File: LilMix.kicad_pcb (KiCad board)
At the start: 2 copper layers, 79.6 x 94.4 mm, 59 parts, among them J1_L1 MONO, J1_R1 MONO, J2_L1 MONO, J2_R1 MONO, J3 STEREO, J4 MONO, J5 MONO, J6 STEREO, U1 TL074, U2 NE5532

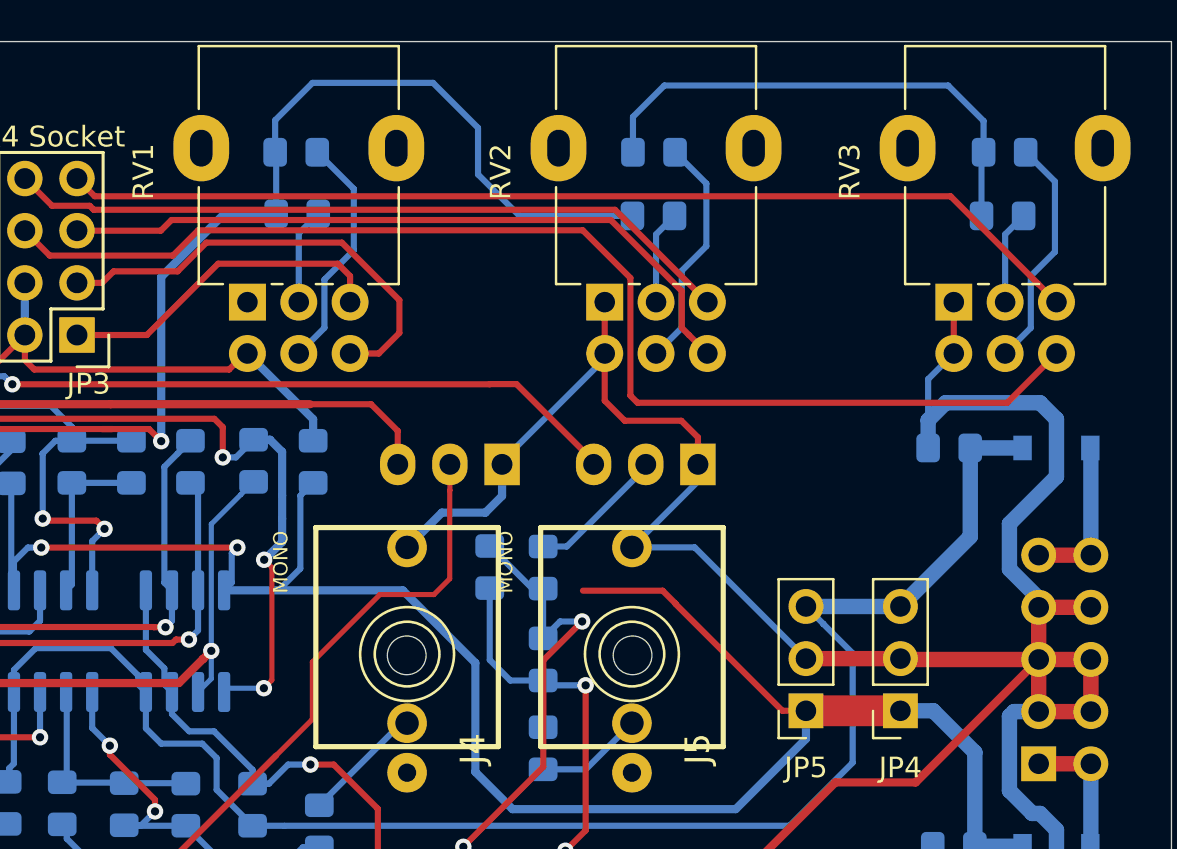
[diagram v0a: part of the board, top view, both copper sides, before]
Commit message: Added another +12v socket header. Initial routing completed
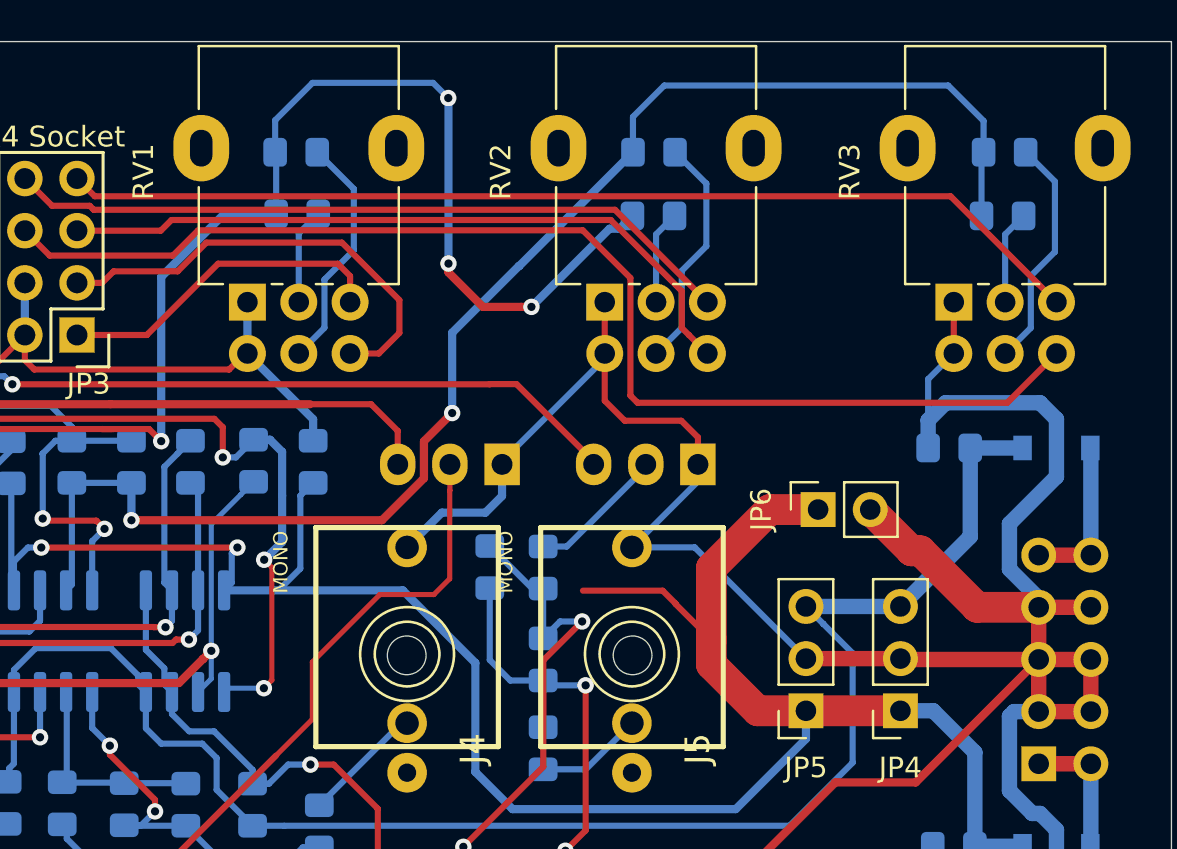
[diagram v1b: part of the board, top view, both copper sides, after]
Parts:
- added JP6: Conn_01x02, Connector_PinSocket_2.54mm:PinSocket_1x02_P2.54mm_Vertical, F.Cu at (151.8, 87.4)
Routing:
- net Net-(C7-Pad2): track 33.1 -> 70.1 mm, vias 0 -> 2
- net GND: track 304.1 -> 316.8 mm
- net +12V: track 96.7 -> 107.2 mm
- net Net-(C6-Pad2): track 64.7 -> 72.1 mm, vias 2 -> 5
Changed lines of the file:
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@@
     (thickness 1.6)
     (drawings 22)
-    (tracks 608)
+    (tracks 642)
     (zones 0)
-    (modules 59)
+    (modules 60)
     (nets 55)
   )
@@
   )
   (setup
-    (last_trace_width 0.3)
+    (last_trace_width 0.4)
     (user_trace_width 0.3)
     (user_trace_width 0.4)
@@
     (add_net R_INV)
   )
+  (module Connector_PinSocket_2.54mm:PinSocket_1x02_P2.54mm_Vertical (layer F.Cu)
+    (at 151.79 87.4 90)
+    (descr "Through hole straight socket strip, 1x02, 2.54mm pitch, single row (from Kicad 4.0.7), script generated")
+    (tags "Through hole socket strip THT 1x02 2.54mm single row")
+    (fp_text reference JP6 (at 0 -2.77 90) (layer F.SilkS)
+      (effects (font (size 1 1) (thickness 0.15)))
+    )
+    (fp_text value Conn_01x02 (at 0 5.31 90) (layer F.Fab)
+      (effects (font (size 1 1) (thickness 0.15)))
+    )
+    (fp_text user %R (at 0 1.27) (layer F.Fab)
+      (effects (font (size 1 1) (thickness 0.15)))
+    )
+    (fp_line (start -1.8 4.3) (end -1.8 -1.8) (layer F.CrtYd) (width 0.05))
+    (fp_line (start 1.75 4.3) (end -1.8 4.3) (layer F.CrtYd) (width 0.05))
+    (fp_line (start 1.75 -1.8) (end 1.75 4.3) (layer F.CrtYd) (width 0.05))
+    (fp_line (start -1.8 -1.8) (end 1.75 -1.8) (layer F.CrtYd) (width 0.05))
+    (fp_line (start 0 -1.33) (end 1.33 -1.33) (layer F.SilkS) (width 0.12))
+    (fp_line (start 1.33 -1.33) (end 1.33 0) (layer F.SilkS) (width 0.12))
+    (fp_line (start 1.33 1.27) (end 1.33 3.87) (layer F.SilkS) (width 0.12))
+    (fp_line (start -1.33 3.87) (end 1.33 3.87) (layer F.SilkS) (width 0.12))
+    (fp_line (start -1.33 1.27) (end -1.33 3.87) (layer F.SilkS) (width 0.12))
+    (fp_line (start -1.33 1.27) (end 1.33 1.27) (layer F.SilkS) (width 0.12))
+    (fp_line (start -1.27 3.81) (end -1.27 -1.27) (layer F.Fab) (width 0.1))
+    (fp_line (start 1.27 3.81) (end -1.27 3.81) (layer F.Fab) (width 0.1))
+    (fp_line (start 1.27 -0.635) (end 1.27 3.81) (layer F.Fab) (width 0.1))
+    (fp_line (start 0.635 -1.27) (end 1.27 -0.635) (layer F.Fab) (width 0.1))
+    (fp_line (start -1.27 -1.27) (end 0.635 -1.27) (layer F.Fab) (width 0.1))
+    (pad 2 thru_hole oval (at 0 2.54 90) (size 1.7 1.7) (drill 1) (layers *.Cu *.Mask)
+      (net 42 GND))
+    (pad 1 thru_hole rect (at 0 0 90) (size 1.7 1.7) (drill 1) (layers *.Cu *.Mask)
+      (net 1 +12V))
+    (model ${KISYS3DMOD}/Connector_PinSocket_2.54mm.3dshapes/PinSocket_1x02_P2.54mm_Vertical.wrl
+      (at (xyz 0 0 0))
+      (scale (xyz 1 1 1))
+      (rotate (xyz 0 0 0))
+    )
+  )
   (module Capacitor_THT:C_Rect_L7.0mm_W4.5mm_P5.00mm (layer F.Cu)
     (at 142.49 156.33 90)
@@
   (segment (start 125.515 91.335) (end 122.865 91.335) (width 0.3) (layer B.Cu) (net 1))
   (segment (start 126.576628 90.273372) (end 125.515 91.335) (width 0.3) (layer B.Cu) (net 1))
-  (segment (start 150.05 97.2) (end 144.85 92) (width 0.3) (layer F.Cu) (net 1))
-  (segment (start 151.2 97.2) (end 150.05 97.2) (width 0.3) (layer F.Cu) (net 1))
   (segment (start 144.85 92) (end 144.85 91.98) (width 0.3) (layer F.Cu) (net 1))
   (segment (start 144.85 91.98) (end 144.22 91.35) (width 0.3) (layer F.Cu) (net 1))
@@
   (segment (start 112.63 89.93) (end 112.63 91.335) (width 0.3) (layer B.Cu) (net 1))
   (segment (start 113.31 89.25) (end 112.63 89.93) (width 0.3) (layer B.Cu) (net 1))
+  (segment (start 146.595 90.245) (end 146.595 93.745) (width 1.5) (layer F.Cu) (net 1))
+  (segment (start 149.44 87.4) (end 146.595 90.245) (width 1.5) (layer F.Cu) (net 1))
+  (segment (start 151.79 87.4) (end 149.44 87.4) (width 1.5) (layer F.Cu) (net 1))
+  (segment (start 146.595 93.745) (end 144.85 92) (width 0.3) (layer F.Cu) (net 1))
+  (segment (start 146.595 94.945) (end 146.595 93.745) (width 1.5) (layer F.Cu) (net 1))
+  (segment (start 148.85 97.2) (end 146.595 94.945) (width 1.5) (layer F.Cu) (net 1))
+  (segment (start 151.2 97.2) (end 148.85 97.2) (width 1.5) (layer F.Cu) (net 1))
   (segment (start 161.75 84.4) (end 159.2 84.4) (width 0.75) (layer B.Cu) (net 2))
   (segment (start 159.2 88.72) (end 155.8 92.12) (width 0.75) (layer B.Cu) (net 2))
@@
   (segment (start 125.35 70) (end 125.35 68.44) (width 0.3) (layer B.Cu) (net 3))
   (segment (start 127.17 66.62) (end 133.04 66.62) (width 0.3) (layer B.Cu) (net 3))
-  (segment (start 133.04 66.62) (end 135.23 68.81) (width 0.3) (layer B.Cu) (net 3))
-  (segment (start 135.23 68.81) (end 135.23 71.08) (width 0.3) (layer B.Cu) (net 3))
+  (segment (start 133.04 66.62) (end 133.78 67.36) (width 0.3) (layer B.Cu) (net 3))
   (segment (start 119.21002 83.48002) (end 119.8 84.07) (width 0.3) (layer F.Cu) (net 3))
-  (segment (start 137.25 73.1) (end 142.75 73.1) (width 0.3) (layer B.Cu) (net 3))
-  (segment (start 135.23 71.08) (end 137.25 73.1) (width 0.3) (layer B.Cu) (net 3))
   (segment (start 116.92002 83.48002) (end 117.43002 83.48002) (width 0.3) (layer F.Cu) (net 3))
   (segment (start 116.92002 83.48002) (end 119.21002 83.48002) (width 0.3) (layer F.Cu) (net 3))
@@
   (segment (start 119.8 76.07) (end 122.87 73) (width 0.4) (layer B.Cu) (net 3))
   (segment (start 125.35 68.44) (end 127.17 66.62) (width 0.3) (layer B.Cu) (net 3))
+  (segment (start 142.126628 73.723372) (end 141.636628 73.723372) (width 0.4) (layer B.Cu) (net 3))
+  (segment (start 142.75 73.1) (end 142.126628 73.723372) (width 0.4) (layer B.Cu) (net 3))
+  (segment (start 141.636628 73.723372) (end 137.83 77.53) (width 0.4) (layer B.Cu) (net 3))
+  (segment (start 137.83 77.53) (end 137.83 77.53) (width 0.4) (layer B.Cu) (net 3))
+  (via (at 133.78 67.36) (size 0.8) (drill 0.4) (layers F.Cu B.Cu) (net 3))
+  (segment (start 133.79 75.42) (end 133.79 75.42) (width 0.4) (layer F.Cu) (net 3))
+  (via (at 133.79 75.42) (size 0.8) (drill 0.4) (layers F.Cu B.Cu) (net 3))
+  (segment (start 133.79 67.37) (end 133.78 67.36) (width 0.4) (layer B.Cu) (net 3))
+  (segment (start 133.79 75.42) (end 133.79 67.37) (width 0.4) (layer B.Cu) (net 3))
+  (via (at 137.83 77.53) (size 0.8) (drill 0.4) (layers F.Cu B.Cu) (net 3))
+  (segment (start 137.34 77.53) (end 137.83 77.53) (width 0.4) (layer F.Cu) (net 3))
+  (segment (start 135.47 77.53) (end 137.34 77.53) (width 0.4) (layer F.Cu) (net 3))
+  (segment (start 133.79 75.42) (end 133.79 75.85) (width 0.4) (layer F.Cu) (net 3))
+  (segment (start 133.79 75.85) (end 135.47 77.53) (width 0.4) (layer F.Cu) (net 3))
   (segment (start 104.876628 85.626628) (end 105.5 86.25) (width 0.3) (layer B.Cu) (net 4))
   (segment (start 103.65 84.4) (end 104.876628 85.626628) (width 0.3) (layer B.Cu) (net 4))
@@
   (segment (start 115.45 91.055) (end 115.17 91.335) (width 0.3) (layer B.Cu) (net 5))
   (segment (start 115.45 86.1) (end 115.45 91.055) (width 0.3) (layer B.Cu) (net 5))
+  (segment (start 118.35 86.1) (end 118.35 87.92) (width 0.4) (layer B.Cu) (net 5))
+  (segment (start 118.35 87.92) (end 118.35 87.92) (width 0.4) (layer B.Cu) (net 5))
+  (via (at 118.35 87.92) (size 0.8) (drill 0.4) (layers F.Cu B.Cu) (net 5))
+  (segment (start 132.59639 85.875804) (end 132.59639 84.07361) (width 0.4) (layer F.Cu) (net 5))
+  (segment (start 118.35 87.92) (end 130.552194 87.92) (width 0.4) (layer F.Cu) (net 5))
+  (segment (start 130.552194 87.92) (end 132.59639 85.875804) (width 0.4) (layer F.Cu) (net 5))
+  (segment (start 132.59639 84.07361) (end 133.97 82.7) (width 0.4) (layer F.Cu) (net 5))
+  (segment (start 133.97 82.7) (end 133.97 82.7) (width 0.4) (layer F.Cu) (net 5))
+  (via (at 133.97 82.7) (size 0.8) (drill 0.4) (layers F.Cu B.Cu) (net 5))
+  (segment (start 137.235 75.54) (end 142.775 70) (width 0.4) (layer B.Cu) (net 5))
+  (segment (start 137.235 75.54) (end 137.22 75.54) (width 0.4) (layer B.Cu) (net 5))
+  (segment (start 133.97 78.79) (end 133.97 82.7) (width 0.4) (layer B.Cu) (net 5))
+  (segment (start 137.22 75.54) (end 133.97 78.79) (width 0.4) (layer B.Cu) (net 5))
   (segment (start 118.35 84.05) (end 115.45 84.05) (width 0.3) (layer B.Cu) (net 6))
   (segment (start 116.44 91.335) (end 116.44 88.94) (width 0.3) (layer B.Cu) (net 6))
@@
   (segment (start 111.36 91.335) (end 111.36 92.92) (width 0.3) (layer B.Cu) (net 42))
   (segment (start 111.36 92.92) (end 111.78 93.34) (width 0.3) (layer B.Cu) (net 42))
+  (segment (start 154.33 87.4) (end 156.34 89.41) (width 1.5) (layer F.Cu) (net 42))
+  (segment (start 156.34 89.41) (end 156.78 89.41) (width 1.5) (layer F.Cu) (net 42))
+  (segment (start 159.53 92.16) (end 162.535 92.16) (width 1.5) (layer F.Cu) (net 42))
+  (segment (start 156.78 89.41) (end 159.53 92.16) (width 1.5) (layer F.Cu) (net 42))
+  (segment (start 124 79.8) (end 124 77.3) (width 0.4) (layer B.Cu) (net 42))
   (segment (start 96.69 152.59) (end 96.69 153.811314) (width 0.5) (layer F.Cu) (net 43))
   (segment (start 98.828686 155.95) (end 104.95 155.95) (width 0.5) (layer F.Cu) (net 43))

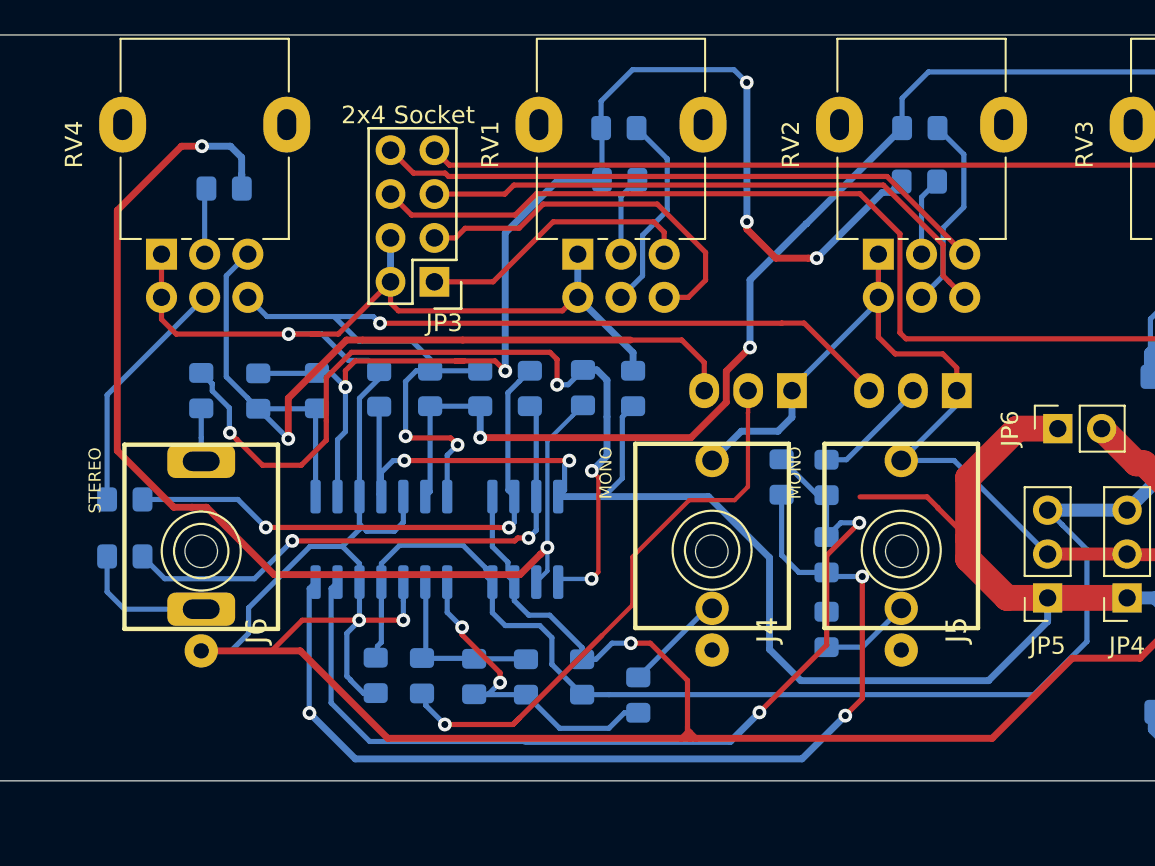
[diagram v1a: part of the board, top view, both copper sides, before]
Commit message: Removed extra tracks and vias. Increased trace sizes around the board
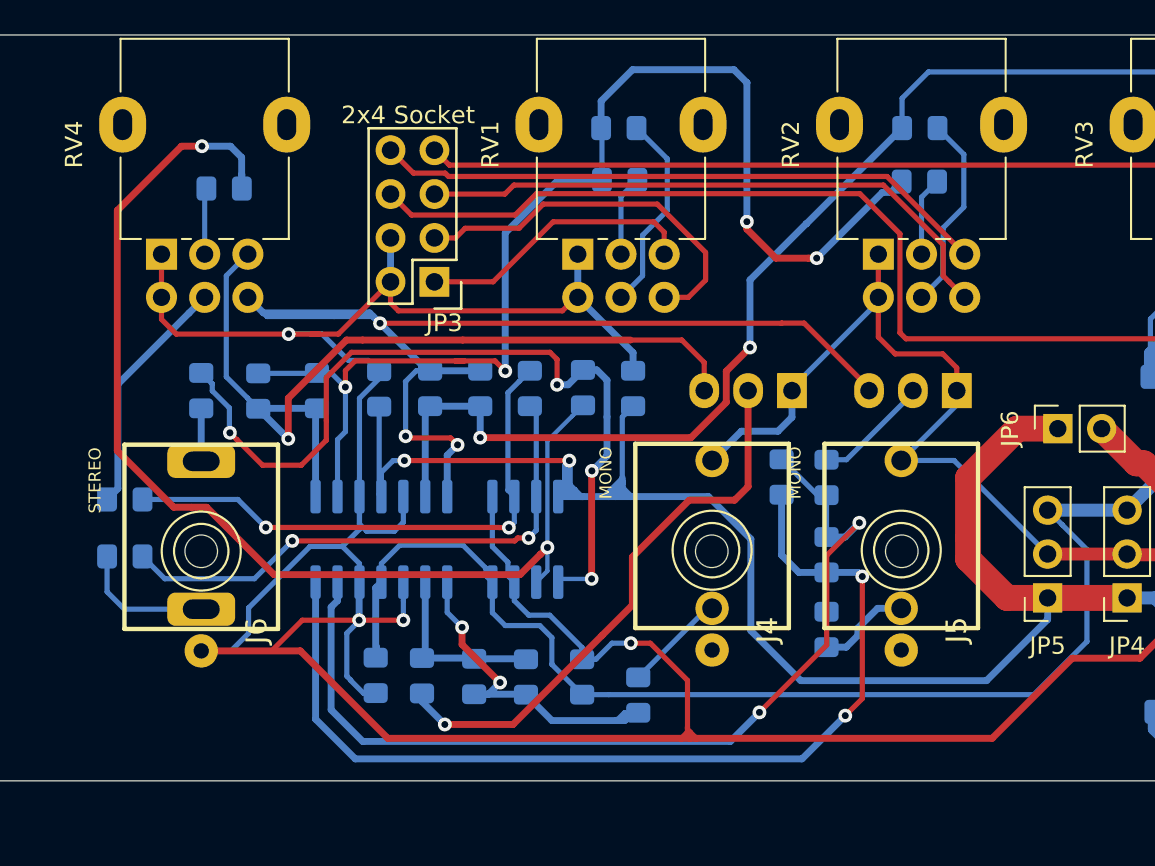
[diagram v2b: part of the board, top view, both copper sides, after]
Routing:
- net Net-(R11-Pad2): track 33.1 -> 42.7 mm
- net R_INV: track 59.8 -> 64.8 mm
- net Net-(C9-Pad2): track 10.2 -> 13.4 mm
- net GND: track 316.8 -> 319.0 mm
- net +12V: track 107.2 -> 106.0 mm
- net Net-(C9-Pad1): track 19.6 -> 20.6 mm
- net Net-(C6-Pad2): track 72.1 -> 73.1 mm, vias 5 -> 4
- net -12V: track 78.7 -> 79.4 mm
- net Net-(C10-Pad1): track 60.3 -> 60.0 mm, vias 3 -> 2

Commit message: Flipped power headers
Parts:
- JP4, JP5, JP6: moved to B.Cu
- turned JP4 to 0 degrees
- turned JP5 to 0 degrees
- turned JP6 to 270 degrees
